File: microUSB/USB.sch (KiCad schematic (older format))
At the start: 32 parts, among them J1 Conn_02x12_Odd_Even, J2 Conn_02x06_Odd_Even

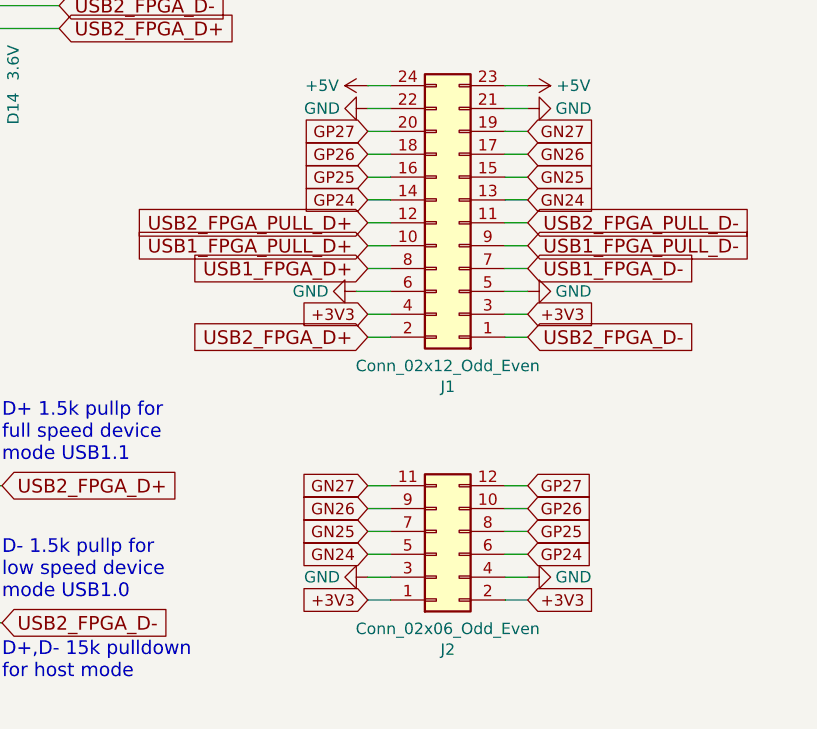
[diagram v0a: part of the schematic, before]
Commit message: Adding missing connections
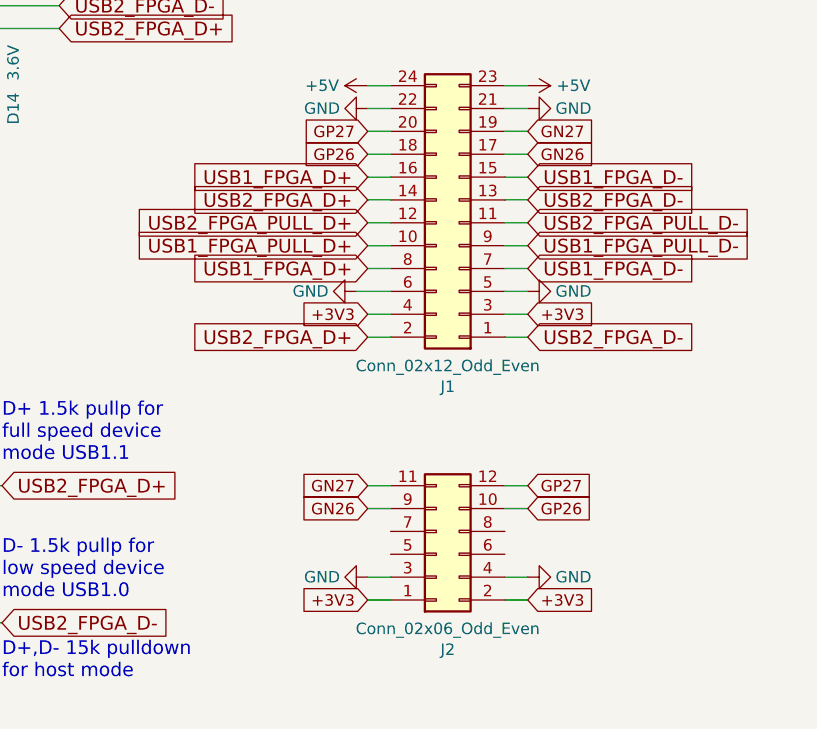
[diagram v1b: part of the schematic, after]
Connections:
- net GN24: no longer J1.13 (Pin_13), J2.5 (Pin_5)
- net GP24: no longer J1.14 (Pin_14), J2.6 (Pin_6)
- net USB1_FPGA_D+: now also J1.16 (Pin_16)
- net USB1_FPGA_D-: now also J1.15 (Pin_15)
- net USB2_FPGA_D+: now also J1.14 (Pin_14)
- net USB2_FPGA_D-: now also J1.13 (Pin_13)
- net GN25: no longer names the net of J2.7 (Pin_7)
- net GN25: no longer J1.15 (Pin_15)
- net GP25: no longer names the net of J2.8 (Pin_8)
- net GP25: no longer J1.16 (Pin_16)
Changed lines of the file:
@@
 Text GLabel 9750 2750 2    50   Input ~ 0
 GN26
-Text GLabel 9750 2850 2    50   Input ~ 0
-GN25
-Text GLabel 9750 2950 2    50   Input ~ 0
-GN24
 Text GLabel 9750 3450 2    50   Input ~ 0
 +3V3
@@
 Text GLabel 9050 2750 0    50   Input ~ 0
 GP26
-Text GLabel 9050 2850 0    50   Input ~ 0
-GP25
-Text GLabel 9050 2950 0    50   Input ~ 0
-GP24
 Text GLabel 9050 3450 0    50   Input ~ 0
 +3V3
@@
 Text GLabel 9050 4300 0    50   Input ~ 0
 GN26
-Text GLabel 9050 4400 0    50   Input ~ 0
-GN25
-Text GLabel 9050 4500 0    50   Input ~ 0
-GN24
 Text GLabel 9750 4200 2    50   Input ~ 0
 GP27
 Text GLabel 9750 4300 2    50   Input ~ 0
 GP26
-Text GLabel 9750 4400 2    50   Input ~ 0
-GP25
-Text GLabel 9750 4500 2    50   Input ~ 0
-GP24
 Wire Wire Line
 	9050 4200 9150 4200
@@
 	9050 4300 9150 4300
 Wire Wire Line
-	9050 4400 9150 4400
-Wire Wire Line
-	9050 4500 9150 4500
-Wire Wire Line
 	9050 4600 9150 4600
 Wire Wire Line
@@
 Wire Wire Line
 	9650 4300 9750 4300
-Wire Wire Line
-	9650 4400 9750 4400
-Wire Wire Line
-	9650 4500 9750 4500
 Wire Wire Line
 	9650 4600 9750 4600
@@
 	1    0    0    1
 $EndComp
+Text GLabel 9050 2950 0    60   Input ~ 0
+USB2_FPGA_D+
+Text GLabel 9050 2850 0    60   Input ~ 0
+USB1_FPGA_D+
+Text GLabel 9750 2950 2    60   Input ~ 0
+USB2_FPGA_D-
+Text GLabel 9750 2850 2    60   Input ~ 0
+USB1_FPGA_D-
 $EndSCHEMATC
